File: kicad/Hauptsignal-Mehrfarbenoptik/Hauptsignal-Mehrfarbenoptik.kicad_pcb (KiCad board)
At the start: 2 copper layers, 6.6 x 13.6 mm, 17 parts, among them J0 VCC, J1 VkzBw, J2 ARGB_2, J3 ARGB_3, J4 ARGB_4, J5 Zs7-3, J6 Ra, J7 Zs7-1, J8 Zs7-2, J9 Ra/Zs1

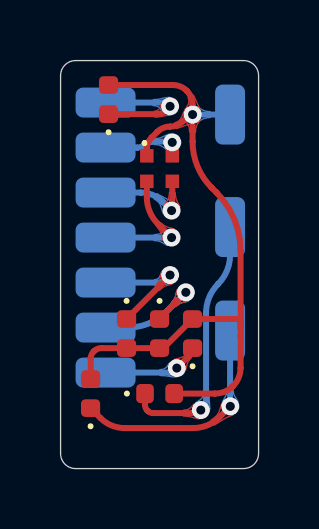
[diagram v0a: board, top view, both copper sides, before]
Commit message: feat: re-route MSO
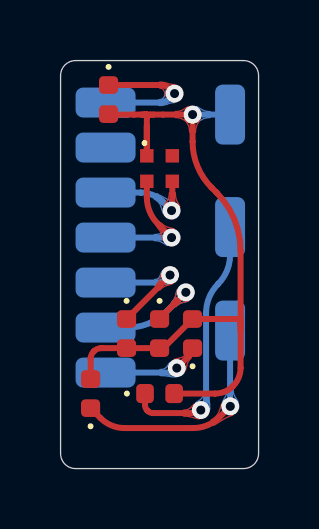
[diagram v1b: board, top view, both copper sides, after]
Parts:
- turned D1 to -90 degrees
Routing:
- net Net-(D2-Pad2): track 2.73 -> 0.00 mm, vias 1 -> 0
- net Net-(D1-Pad2): track 24.4 -> 23.9 mm

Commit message: fix: MSO missing trace
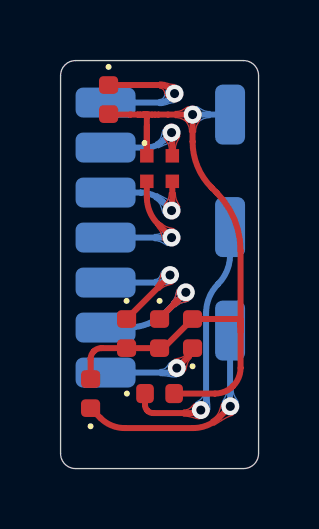
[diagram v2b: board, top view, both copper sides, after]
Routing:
- net Net-(D2-Pad2): track 0.00 -> 3.15 mm, vias 0 -> 1

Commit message: Add CC-BY-SA 4.0 license
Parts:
- moved J1 24.3 mm to (101.0, 61.4)
- moved J2 24.3 mm to (101.0, 62.9)
- moved D1 24.3 mm to (101.1, 61.3)
- moved D10 24.3 mm to (100.5, 71.1)
- moved D6 24.3 mm to (101.7, 69.1)
- moved D7 24.3 mm to (102.8, 69.1)
- moved D8 24.3 mm to (103.9, 69.1)
- moved D9 24.3 mm to (102.8, 71.1)
- moved J0 24.3 mm to (105.2, 61.8)
- moved J3 24.3 mm to (101.0, 64.4)
- moved J4 24.3 mm to (101.0, 65.9)
- moved J5 24.3 mm to (101.0, 67.4)
- moved J6 24.3 mm to (101.0, 68.9)
- moved J7 24.3 mm to (101.0, 70.4)
- moved J8 24.3 mm to (105.2, 65.5)
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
